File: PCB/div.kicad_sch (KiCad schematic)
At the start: 32 parts, among them J2 Bus Gate Reset, Q4 BC557, U1 4024

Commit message: :art: Change the diode footprint to make soldering easier
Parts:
- D? (x3): footprint Diode_THT:D_DO-35_SOD27_P7.62mm_Horizontal -> moPsy:D_DO-35_SOD27_P5.08mm_Horizontal
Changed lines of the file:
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@@
       (effects (font (size 1.27 1.27)))
     )
-    (property "Footprint" "Diode_THT:D_DO-35_SOD27_P7.62mm_Horizontal" (at 47.625 113.03 0)
+    (property "Footprint" "moPsy:D_DO-35_SOD27_P5.08mm_Horizontal" (at 47.625 113.03 0)
       (effects (font (size 1.27 1.27)) hide)
     )
@@
       (effects (font (size 1.27 1.27)))
     )
-    (property "Footprint" "Diode_THT:D_DO-35_SOD27_P7.62mm_Horizontal" (at 57.785 133.35 0)
+    (property "Footprint" "moPsy:D_DO-35_SOD27_P5.08mm_Horizontal" (at 57.785 133.35 0)
       (effects (font (size 1.27 1.27)) hide)
     )
@@
       (effects (font (size 1.27 1.27)))
     )
-    (property "Footprint" "Diode_THT:D_DO-35_SOD27_P7.62mm_Horizontal" (at 55.245 53.975 0)
-      (effects (font (size 1.27 1.27)) hide)
-    )
+    (property "Footprint" "moPsy:D_DO-35_SOD27_P5.08mm_Horizontal" (at 55.245 53.975 0)
+      (effects (font (size 1.27 1.27)) hide)
+    )

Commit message: :lipstick: Perform a Geographical Reannotation on the PCB
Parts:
- renumbered J2 to J1
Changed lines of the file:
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@@
       (project "div"
         (path "/69636855-5bea-4b1f-bae0-d5724c7c5e69"
-          (reference "R28") (unit 1)
+          (reference "R10") (unit 1)
         )
       )
@@
       (project "div"
         (path "/69636855-5bea-4b1f-bae0-d5724c7c5e69"
-          (reference "C3") (unit 1)
+          (reference "C1") (unit 1)
         )
       )
@@
       (project "div"
         (path "/69636855-5bea-4b1f-bae0-d5724c7c5e69"
-          (reference "D2") (unit 1)
+          (reference "D17") (unit 1)
         )
       )
@@
       (project "div"
         (path "/69636855-5bea-4b1f-bae0-d5724c7c5e69"
-          (reference "D6") (unit 1)
+          (reference "D1") (unit 1)
         )
         (path "/69636855-5bea-4b1f-bae0-d5724c7c5e69/ddb23b62-aa27-4614-8e08-b908b2a2dd99"
@@
       (project "div"
         (path "/69636855-5bea-4b1f-bae0-d5724c7c5e69"
-          (reference "R8") (unit 1)
+          (reference "R1") (unit 1)
         )
         (path "/69636855-5bea-4b1f-bae0-d5724c7c5e69/ddb23b62-aa27-4614-8e08-b908b2a2dd99"
@@
       (project "div"
         (path "/69636855-5bea-4b1f-bae0-d5724c7c5e69"
-          (reference "R5") (unit 1)
+          (reference "R7") (unit 1)
         )
       )
@@
       (project "div"
         (path "/69636855-5bea-4b1f-bae0-d5724c7c5e69"
-          (reference "Q2") (unit 1)
+          (reference "Q1") (unit 1)
         )
       )
@@
       (project "div"
         (path "/69636855-5bea-4b1f-bae0-d5724c7c5e69"
-          (reference "J4") (unit 1)
+          (reference "J10") (unit 1)
         )
       )
@@
       (project "div"
         (path "/69636855-5bea-4b1f-bae0-d5724c7c5e69"
-          (reference "R7") (unit 1)
+          (reference "R6") (unit 1)
         )
         (path "/69636855-5bea-4b1f-bae0-d5724c7c5e69/ddb23b62-aa27-4614-8e08-b908b2a2dd99"
@@
       (project "div"
         (path "/69636855-5bea-4b1f-bae0-d5724c7c5e69"
-          (reference "C1") (unit 1)
+          (reference "C3") (unit 1)
         )
       )
@@
       (project "div"
         (path "/69636855-5bea-4b1f-bae0-d5724c7c5e69"
-          (reference "D1") (unit 1)
+          (reference "D5") (unit 1)
         )
       )
@@
       (project "div"
         (path "/69636855-5bea-4b1f-bae0-d5724c7c5e69"
-          (reference "Q3") (unit 1)
+          (reference "Q2") (unit 1)
         )
       )
@@
       (project "div"
         (path "/69636855-5bea-4b1f-bae0-d5724c7c5e69"
-          (reference "Q1") (unit 1)
+          (reference "Q3") (unit 1)
         )
       )
@@
       (project "div"
         (path "/69636855-5bea-4b1f-bae0-d5724c7c5e69"
-          (reference "R27") (unit 1)
+          (reference "R9") (unit 1)
         )
       )
@@
       (project "div"
         (path "/69636855-5bea-4b1f-bae0-d5724c7c5e69"
-          (reference "D20") (unit 1)
+          (reference "D7") (unit 1)
         )
         (path "/69636855-5bea-4b1f-bae0-d5724c7c5e69/ddb23b62-aa27-4614-8e08-b908b2a2dd99"
@@
       (project "div"
         (path "/69636855-5bea-4b1f-bae0-d5724c7c5e69"
-          (reference "R1") (unit 1)
+          (reference "R2") (unit 1)
         )
       )
@@
       (project "div"
         (path "/69636855-5bea-4b1f-bae0-d5724c7c5e69"
-          (reference "D19") (unit 1)
+          (reference "D2") (unit 1)
         )
         (path "/69636855-5bea-4b1f-bae0-d5724c7c5e69/ddb23b62-aa27-4614-8e08-b908b2a2dd99"
@@
       (project "div"
         (path "/69636855-5bea-4b1f-bae0-d5724c7c5e69"
-          (reference "D5") (unit 1)
+          (reference "D6") (unit 1)
         )
         (path "/69636855-5bea-4b1f-bae0-d5724c7c5e69/ddb23b62-aa27-4614-8e08-b908b2a2dd99"
@@
       (project "div"
         (path "/69636855-5bea-4b1f-bae0-d5724c7c5e69"
-          (reference "R2") (unit 1)
+          (reference "R8") (unit 1)
         )
       )
@@
       (project "div"
         (path "/69636855-5bea-4b1f-bae0-d5724c7c5e69"
-          (reference "J3") (unit 1)
+          (reference "J2") (unit 1)
         )
       )
@@
       (project "div"
         (path "/69636855-5bea-4b1f-bae0-d5724c7c5e69"
-          (reference "J1") (unit 1)
+          (reference "J3") (unit 1)
         )
       )
@@
       (project "div"
         (path "/69636855-5bea-4b1f-bae0-d5724c7c5e69"
-          (reference "R6") (unit 1)
+          (reference "R11") (unit 1)
         )
       )
@@
   (symbol (lib_id "Connector:Conn_01x02_Pin") (at 27.94 99.695 270) (unit 1)
     (in_bom yes) (on_board yes) (dnp no)
-    (property "Reference" "J2" (at 22.225 100.33 90)
+    (property "Reference" "J1" (at 22.225 100.33 90)
       (effects (font (size 1.27 1.27)))
     )
@@
       (project "div"
         (path "/69636855-5bea-4b1f-bae0-d5724c7c5e69"
-          (reference "J2") (unit 1)
+          (reference "J1") (unit 1)
         )
       )
@@
       (project "div"
         (path "/69636855-5bea-4b1f-bae0-d5724c7c5e69"
-          (reference "R29") (unit 1)
-        )
-      )
+          (reference "R5") (unit 1)
+        )
+      )

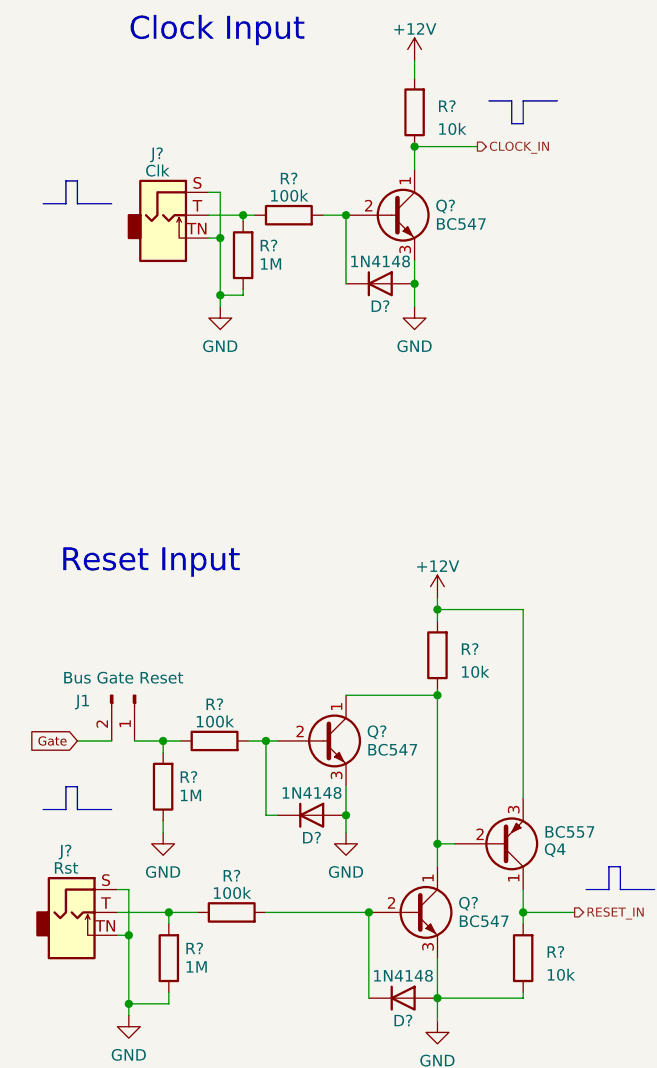
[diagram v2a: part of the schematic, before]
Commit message: :wrench: Revert input resistors to 10K
Test built with SMD LEDs shows that the 100K base resistor does not
open the transistors sufficiently. Change back to 10K for robust
operation.

The problem that occurred: With lower LED series resistors (220R) the
transistor would be part of a voltage divider leading to 6V output,
which is not enough to trigger the 4024 clock input.
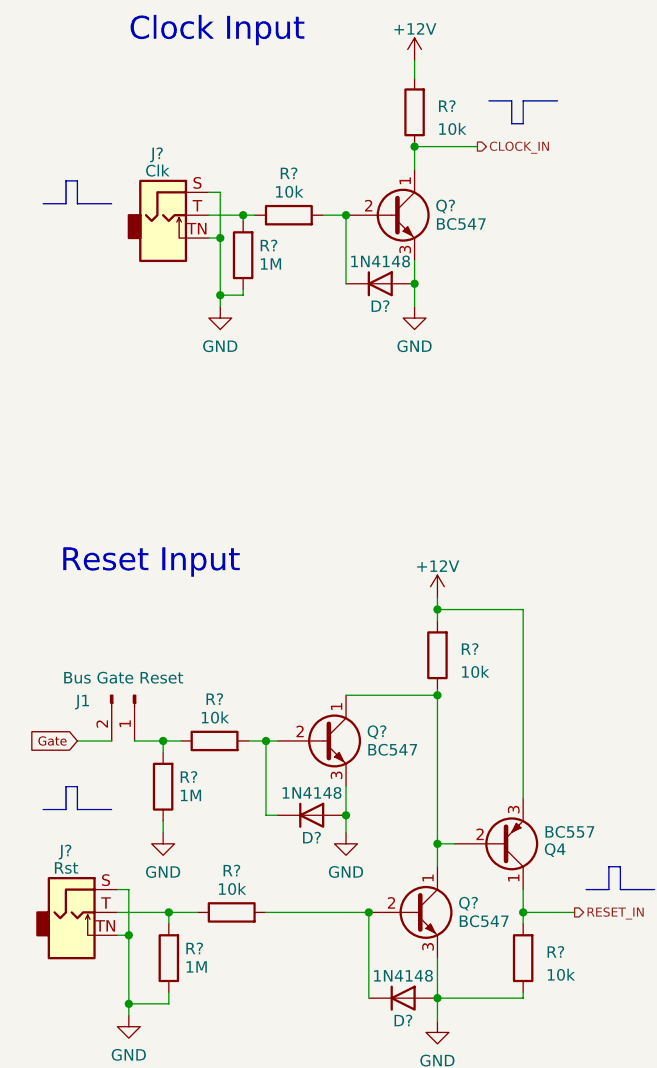
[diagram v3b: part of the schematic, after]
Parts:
- R? (x3): value 100k -> 10k
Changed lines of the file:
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@@
   (symbol (lib_id "Device:R") (at 36.83 104.775 90) (unit 1)
     (in_bom yes) (on_board yes) (dnp no) (fields_autoplaced)
-    (property "Reference" "R?" (at 36.83 100.7491 90)
-      (effects (font (size 1.27 1.27)))
-    )
-    (property "Value" "100k" (at 36.83 102.6701 90)
+    (property "Reference" "R?" (at 36.83 100.179 90)
+      (effects (font (size 1.27 1.27)))
+    )
+    (property "Value" "10k" (at 36.83 102.227 90)
       (effects (font (size 1.27 1.27)))
     )
@@
   (symbol (lib_id "Device:R") (at 38.735 123.825 90) (unit 1)
     (in_bom yes) (on_board yes) (dnp no) (fields_autoplaced)
-    (property "Reference" "R?" (at 38.735 119.7991 90)
-      (effects (font (size 1.27 1.27)))
-    )
-    (property "Value" "100k" (at 38.735 121.7201 90)
+    (property "Reference" "R?" (at 38.735 119.229 90)
+      (effects (font (size 1.27 1.27)))
+    )
+    (property "Value" "10k" (at 38.735 121.277 90)
       (effects (font (size 1.27 1.27)))
     )
@@
   (symbol (lib_id "Device:R") (at 45.085 46.355 90) (unit 1)
     (in_bom yes) (on_board yes) (dnp no) (fields_autoplaced)
-    (property "Reference" "R?" (at 45.085 42.3291 90)
-      (effects (font (size 1.27 1.27)))
-    )
-    (property "Value" "100k" (at 45.085 44.2501 90)
-      (effects (font (size 1.27 1.27)))
-    )
+    (property "Reference" "R?" (at 45.085 41.759 90)
+      (effects (font (size 1.27 1.27)))
+    )
+    (property "Value" "10k" (at 45.085 43.807 90)
+      (effects (font (size 1.27 1.27)))
+    )

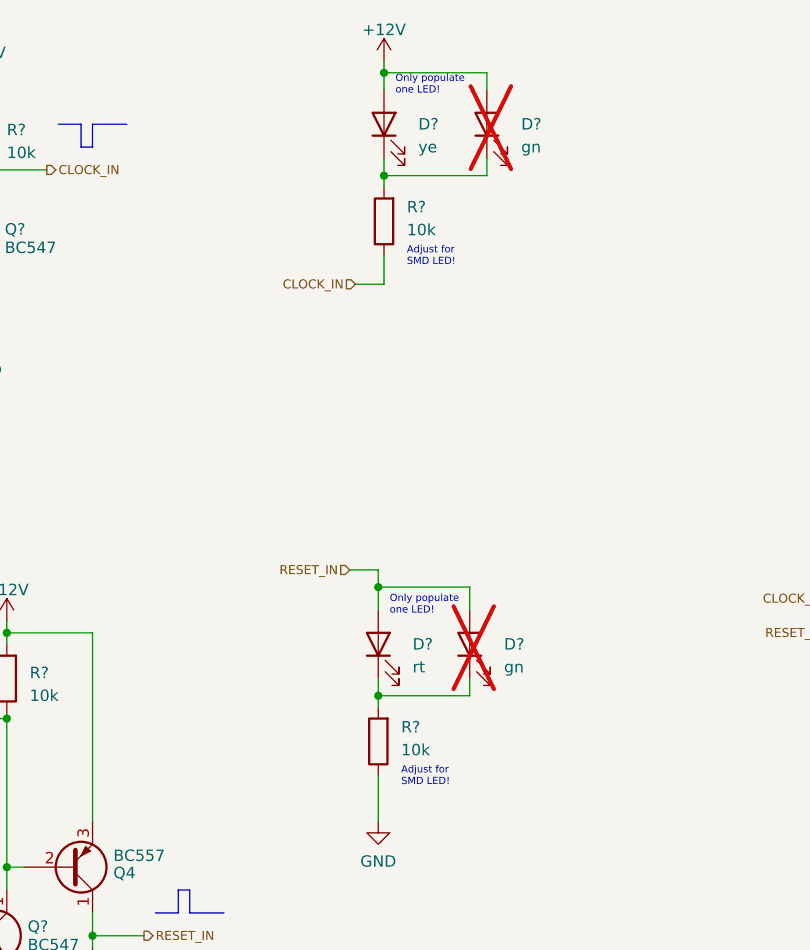
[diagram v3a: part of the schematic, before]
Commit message: :wrench: Change LED footprint to 0603
This is harder to solder, but matching LEDs with 180mcd are available:
* https://www.reichelt.de/led-smd-1608-0603-rot-180-mcd-120--led-el-0603-rt-p156256.html
* https://www.reichelt.de/led-smd-1608-0603-gelb-180-mcd-120--led-el-0603-ge-p156259.html
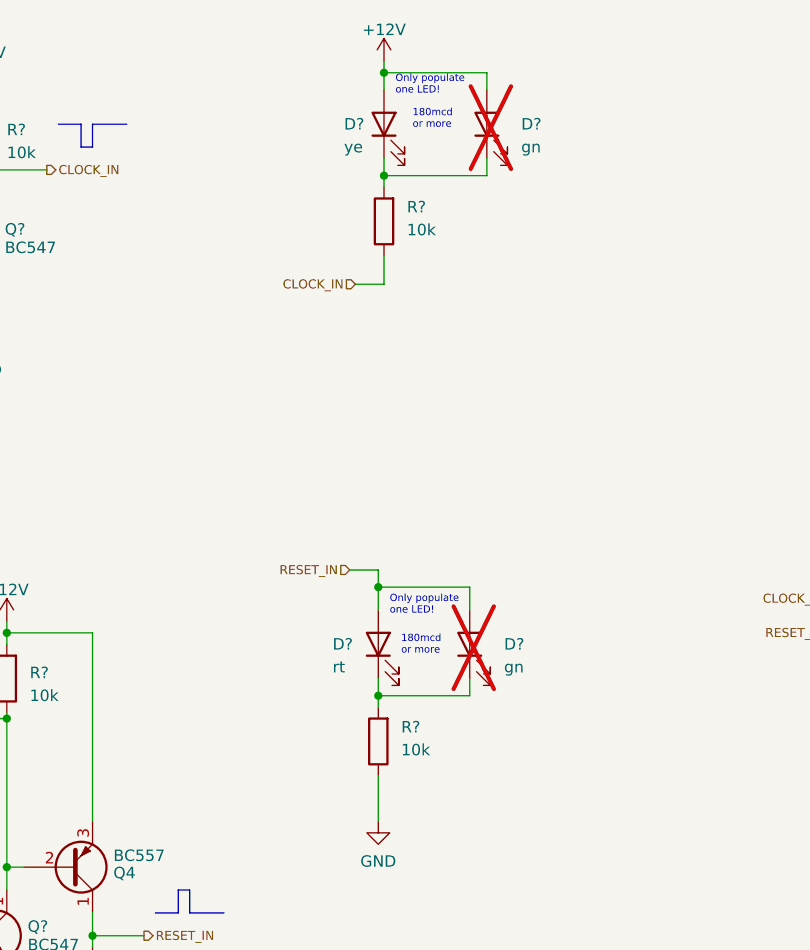
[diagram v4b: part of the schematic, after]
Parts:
- D? (x2): footprint LED_SMD:LED_0805_2012Metric_Pad1.15x1.40mm_HandSolder -> LED_SMD:LED_0603_1608Metric_Pad1.05x0.95mm_HandSolder
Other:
- note added: "180mcd or more"
- note removed: "Adjust for SMD LED!"
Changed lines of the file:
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@@
     (stroke (width 0) (type default))
-  )
-  (text "Adjust for\nSMD LED!" (at 105.41 107.315 0)
-    (effects (font (size 0.8 0.8)) (justify left bottom))
   )
   (text "Gate" (at 30.48 171.45 0)
@@
     (effects (font (size 1 1)) (justify left bottom))
   )
+  (text "180mcd \nor more" (at 105.41 92.71 0)
+    (effects (font (size 0.8 0.8)) (justify left bottom))
+  )
   (text "GND" (at 30.48 186.69 0)
     (effects (font (size 1 1)) (justify right bottom))
   )
-  (text "Adjust for\nSMD LED!" (at 106.045 49.53 0)
+  (text "180mcd \nor more" (at 106.68 34.29 0)
     (effects (font (size 0.8 0.8)) (justify left bottom))
   )
@@
   (symbol (lib_id "Device:LED") (at 103.505 33.655 90) (unit 1)
     (in_bom yes) (on_board yes) (dnp no)
-    (property "Reference" "D?" (at 107.315 33.655 90)
-      (effects (font (size 1.27 1.27)) (justify right))
-    )
-    (property "Value" "ye" (at 107.315 36.195 90)
+    (property "Reference" "D?" (at 99.06 33.655 90)
+      (effects (font (size 1.27 1.27)) (justify right))
+    )
+    (property "Value" "ye" (at 99.06 36.195 90)
       (effects (font (size 1.27 1.27)) (justify right))
     )
@@
       (effects (font (size 1.27 1.27)) (justify right))
     )
-    (property "Footprint" "LED_SMD:LED_0805_2012Metric_Pad1.15x1.40mm_HandSolder" (at 113.03 91.44 0)
+    (property "Footprint" "LED_SMD:LED_0603_1608Metric_Pad1.05x0.95mm_HandSolder" (at 113.03 91.44 0)
       (effects (font (size 1.27 1.27)) hide)
     )
@@
       (effects (font (size 1.27 1.27)) (justify right))
     )
-    (property "Footprint" "LED_SMD:LED_0805_2012Metric_Pad1.15x1.40mm_HandSolder" (at 114.935 33.655 0)
+    (property "Footprint" "LED_SMD:LED_0603_1608Metric_Pad1.05x0.95mm_HandSolder" (at 114.935 33.655 0)
       (effects (font (size 1.27 1.27)) hide)
     )
@@
   (symbol (lib_id "Device:LED") (at 102.87 91.44 90) (unit 1)
     (in_bom yes) (on_board yes) (dnp no)
-    (property "Reference" "D?" (at 106.68 91.44 90)
-      (effects (font (size 1.27 1.27)) (justify right))
-    )
-    (property "Value" "rt" (at 106.68 93.98 90)
-      (effects (font (size 1.27 1.27)) (justify right))
-    )
+    (property "Reference" "D?" (at 97.79 91.44 90)
+      (effects (font (size 1.27 1.27)) (justify right))
+    )
+    (property "Value" "rt" (at 97.79 93.98 90)
+      (effects (font (size 1.27 1.27)) (justify right))
+    )
